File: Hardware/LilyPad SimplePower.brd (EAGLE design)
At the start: 28.4 x 28.4 mm, 16 parts, among them U1 MCP73831

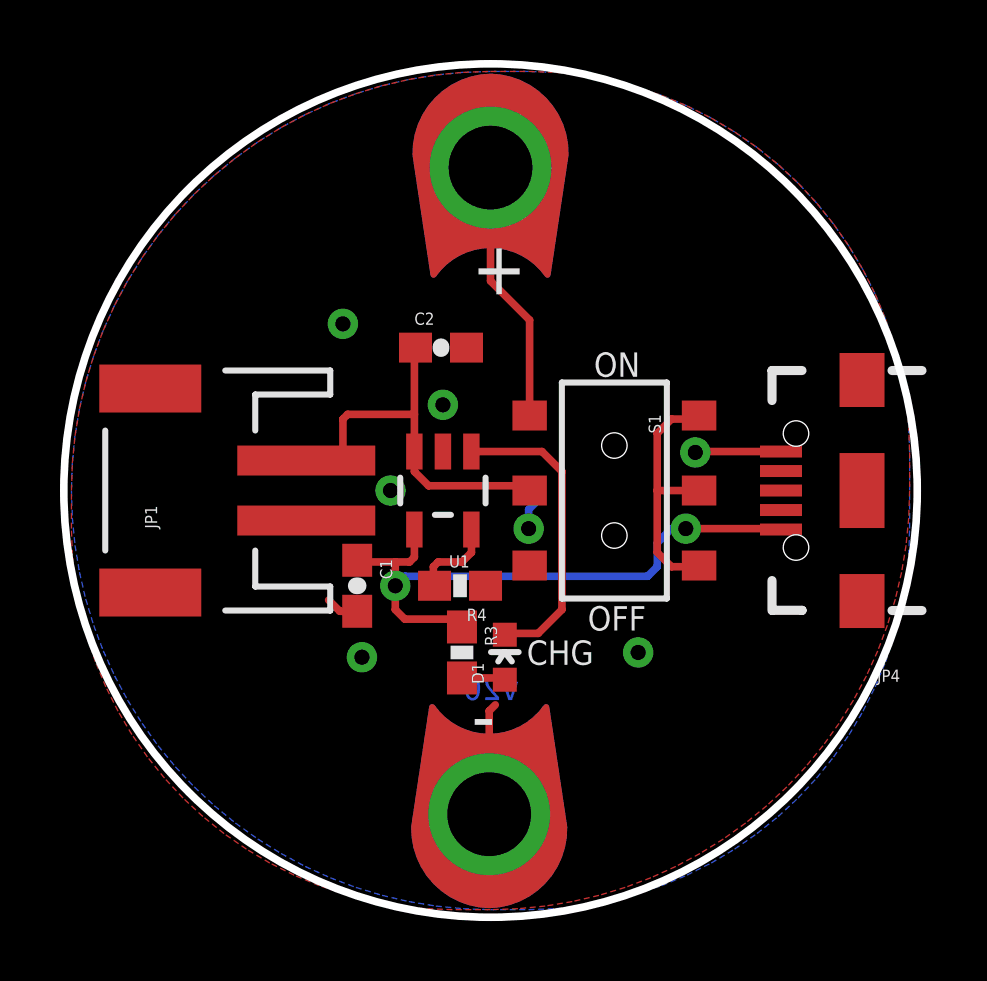
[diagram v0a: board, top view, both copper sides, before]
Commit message: Updating round two protos again to fix missing drill hits.
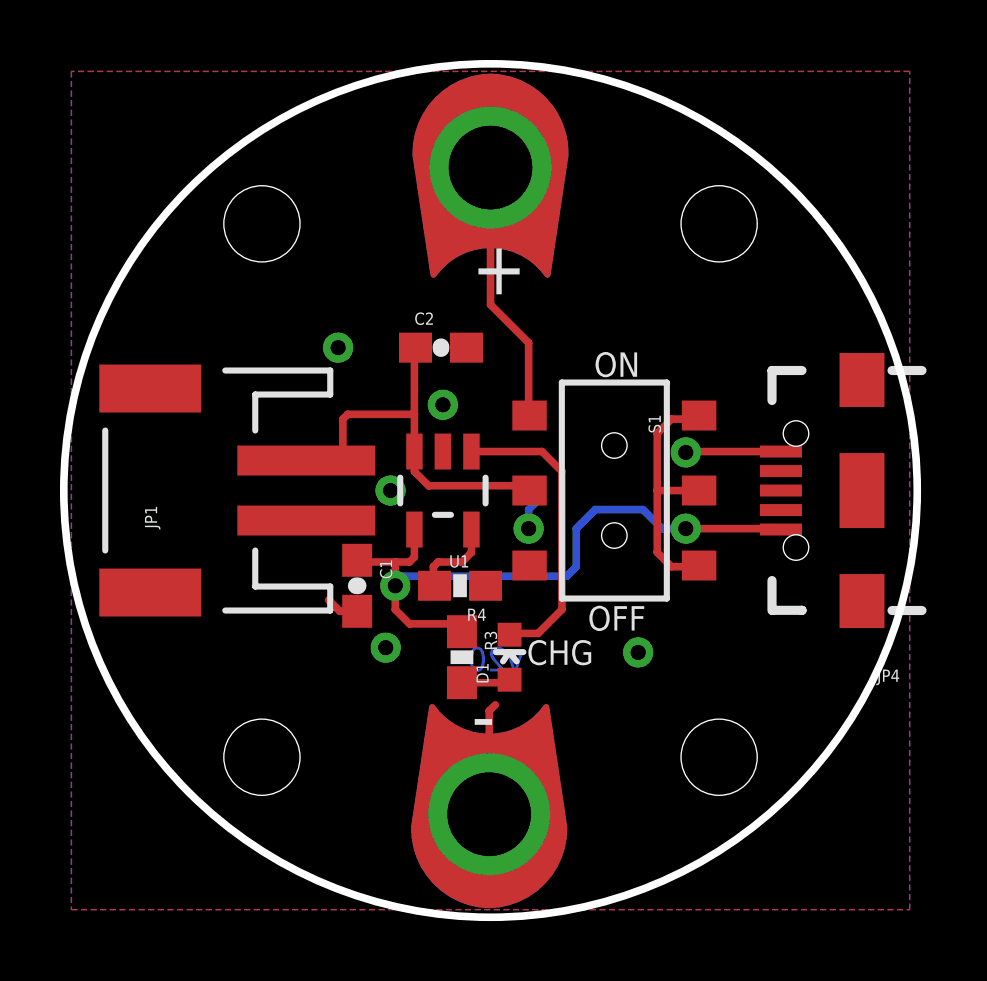
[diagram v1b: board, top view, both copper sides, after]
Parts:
- added STANDOFF1, STANDOFF2, STANDOFF3, STANDOFF4: SEW-HOLE-NO-PAD, Local Library:SEW-HOLE-NO-PAD
- moved JP3 7.68 mm to (-1.11, -5.24)
- moved U$5 6.94 mm to (1.27, -3.81)
- moved U$1 0.32 mm to (0.00, 0.95)
- moved D1 0.16 mm to (0.64, -8.10)
- moved R3 0.16 mm to (-0.95, -8.10)
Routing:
- net GND: track 7.64 -> 11.9 mm
- net N$3: track 21.1 -> 22.0 mm

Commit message: added board fiducials
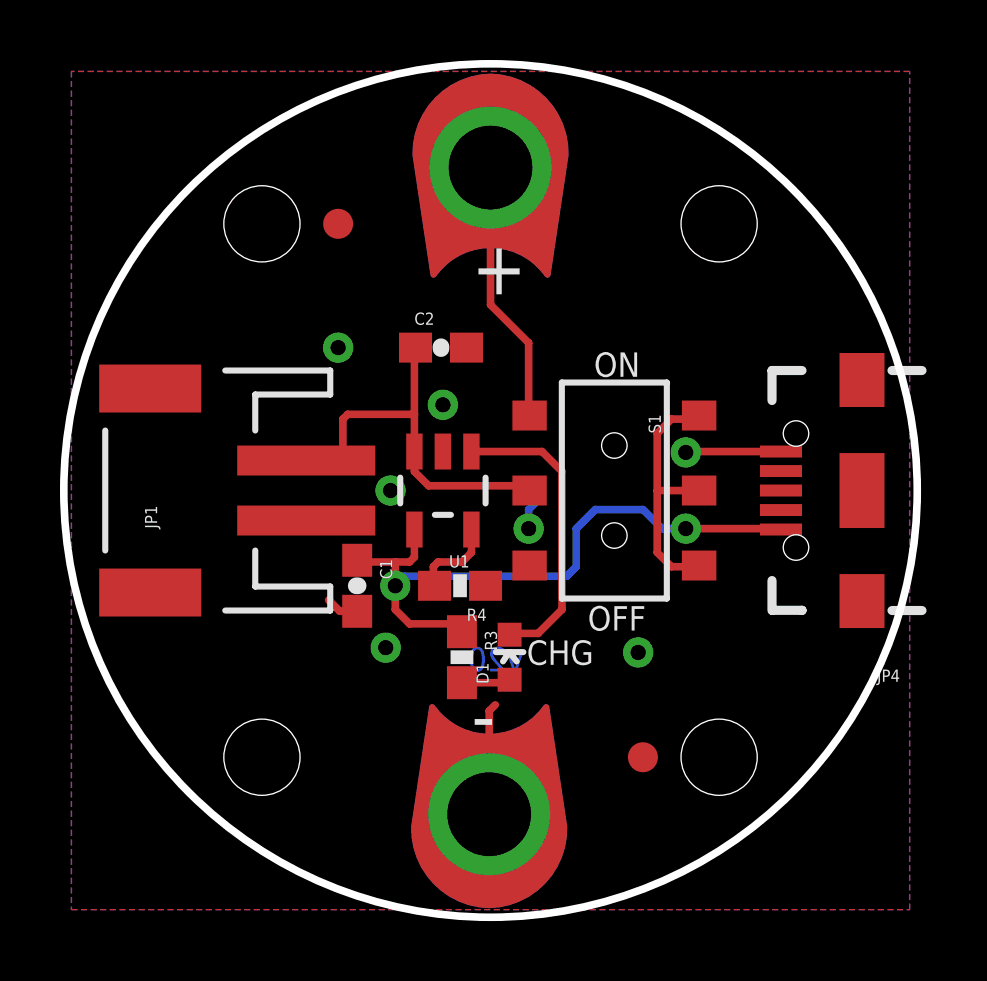
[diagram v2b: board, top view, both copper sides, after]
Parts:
- added FID1, FID2: FIDUCIAL1X2, SparkFun-Aesthetics:FIDUCIAL-1X2
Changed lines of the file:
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@@
 <setting verticaltext="up"/>
 </settings>
-<grid distance="0.00625" unitdist="inch" unit="inch" style="lines" multiple="1" display="yes" altdistance="0.005" altunitdist="inch" altunit="inch"/>
+<grid distance="0.05" unitdist="inch" unit="inch" style="lines" multiple="1" display="yes" altdistance="0.01" altunitdist="inch" altunit="inch"/>
 <layers>
 <layer number="1" name="Top" color="4" fill="1" visible="yes" active="yes"/>
@@
 <layer number="18" name="Vias" color="2" fill="1" visible="yes" active="yes"/>
 <layer number="19" name="Unrouted" color="6" fill="1" visible="yes" active="yes"/>
-<layer number="20" name="Dimension" color="15" fill="1" visible="yes" active="yes"/>
-<layer number="21" name="tPlace" color="16" fill="1" visible="yes" active="yes"/>
-<layer number="22" name="bPlace" color="14" fill="1" visible="yes" active="yes"/>
+<layer number="20" name="Dimension" color="6" fill="1" visible="yes" active="yes"/>
+<layer number="21" name="tPlace" color="6" fill="1" visible="yes" active="yes"/>
+<layer number="22" name="bPlace" color="6" fill="1" visible="yes" active="yes"/>
 <layer number="23" name="tOrigins" color="15" fill="1" visible="yes" active="yes"/>
 <layer number="24" name="bOrigins" color="15" fill="1" visible="yes" active="yes"/>
@@
 <layer number="47" name="Measures" color="7" fill="1" visible="no" active="yes"/>
 <layer number="48" name="Document" color="7" fill="1" visible="no" active="yes"/>
-<layer number="49" name="Reference" color="7" fill="1" visible="yes" active="yes"/>
+<layer number="49" name="Reference" color="7" fill="1" visible="no" active="yes"/>
 <layer number="50" name="dxf" color="7" fill="1" visible="no" active="yes"/>
 <layer number="51" name="tDocu" color="6" fill="1" visible="yes" active="yes"/>
@@
 <element name="STANDOFF3" library="Local Library" package="SEW-HOLE-NO-PAD" value="SEW-HOLE-NO-PAD" x="7.62" y="-11.43"/>
 <element name="STANDOFF4" library="Local Library" package="SEW-HOLE-NO-PAD" value="SEW-HOLE-NO-PAD" x="-7.62" y="-11.43"/>
+<element name="FID1" library="SparkFun-Aesthetics" package="FIDUCIAL-1X2" value="FIDUCIAL1X2" x="-5.08" y="6.35"/>
+<element name="FID2" library="SparkFun-Aesthetics" package="FIDUCIAL-1X2" value="FIDUCIAL1X2" x="5.08" y="-11.43"/>
 </elements>
 <signals>

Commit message: Fixing short, updating parts to match QC checklist
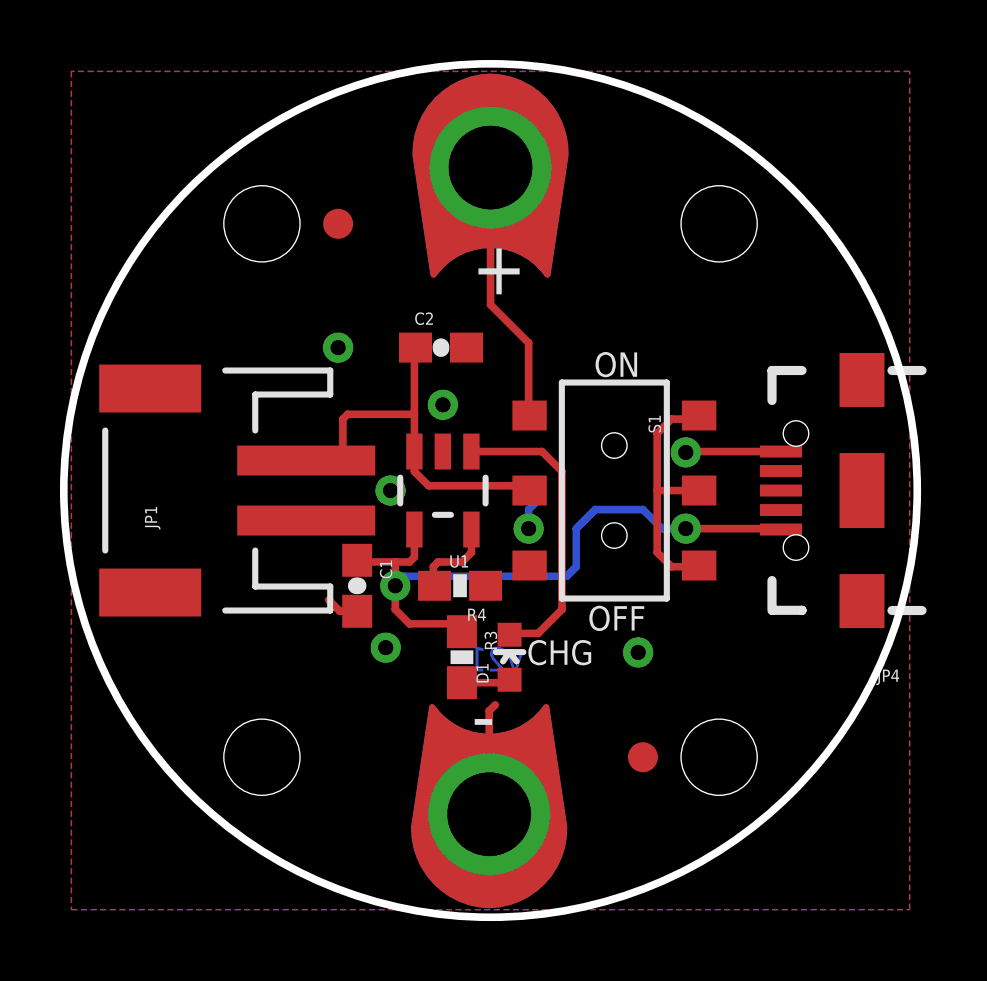
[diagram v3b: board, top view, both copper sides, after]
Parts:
- JP1: value (none) -> M02-JST-2MM-SMT; device SparkFun:JST-2-SMD -> SparkFun-Connectors:JST-2-SMD
- S1: value Power -> DPDT; device SparkFun:AYZ0202 -> SparkFun-Electromechanical:AYZ0202
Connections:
- net N$6 renamed VCC
- net GND: no longer S1.6
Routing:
- net GND: track 11.9 -> 10.7 mm
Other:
- board text added: "v21"
- board text removed: "v20"
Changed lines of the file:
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@@
 <?xml version="1.0" encoding="utf-8"?>
 <!DOCTYPE eagle SYSTEM "eagle.dtd">
-<eagle version="6.6.0">
+<eagle version="7.2.0">
 <drawing>
 <settings>
@@
 <setting verticaltext="up"/>
 </settings>
-<grid distance="0.05" unitdist="inch" unit="inch" style="lines" multiple="1" display="yes" altdistance="0.01" altunitdist="inch" altunit="inch"/>
+<grid distance="0.05" unitdist="inch" unit="inch" style="lines" multiple="1" display="yes" altdistance="0.005" altunitdist="inch" altunit="inch"/>
 <layers>
 <layer number="1" name="Top" color="4" fill="1" visible="yes" active="yes"/>
@@
 <layer number="18" name="Vias" color="2" fill="1" visible="yes" active="yes"/>
 <layer number="19" name="Unrouted" color="6" fill="1" visible="yes" active="yes"/>
-<layer number="20" name="Dimension" color="6" fill="1" visible="yes" active="yes"/>
-<layer number="21" name="tPlace" color="6" fill="1" visible="yes" active="yes"/>
-<layer number="22" name="bPlace" color="6" fill="1" visible="yes" active="yes"/>
+<layer number="20" name="Dimension" color="15" fill="1" visible="yes" active="yes"/>
+<layer number="21" name="tPlace" color="16" fill="1" visible="yes" active="yes"/>
+<layer number="22" name="bPlace" color="14" fill="1" visible="yes" active="yes"/>
 <layer number="23" name="tOrigins" color="15" fill="1" visible="yes" active="yes"/>
 <layer number="24" name="bOrigins" color="15" fill="1" visible="yes" active="yes"/>
@@
 <layer number="47" name="Measures" color="7" fill="1" visible="no" active="yes"/>
 <layer number="48" name="Document" color="7" fill="1" visible="no" active="yes"/>
-<layer number="49" name="Reference" color="7" fill="1" visible="no" active="yes"/>
+<layer number="49" name="Reference" color="7" fill="1" visible="yes" active="yes"/>
 <layer number="50" name="dxf" color="7" fill="1" visible="no" active="yes"/>
 <layer number="51" name="tDocu" color="6" fill="1" visible="yes" active="yes"/>
@@
 <layer number="56" name="wert" color="7" fill="1" visible="no" active="yes"/>
 <layer number="57" name="tCAD" color="7" fill="1" visible="no" active="no"/>
+<layer number="90" name="Modules" color="5" fill="1" visible="no" active="no"/>
 <layer number="91" name="Nets" color="2" fill="1" visible="no" active="no"/>
 <layer number="92" name="Busses" color="1" fill="1" visible="no" active="no"/>
@@
 <text x="-0.635" y="4.0005" size="1.778" layer="21" font="vector" ratio="15">+</text>
 <text x="6.35" y="-26.67" size="1.778" layer="51" font="vector">N. Seidle</text>
-<text x="1.11125" y="-8.5725" size="0.8128" layer="16" font="vector" ratio="25" rot="SMR0">v20</text>
+<text x="1.11125" y="-8.5725" size="0.8128" layer="16" font="vector" ratio="25" rot="SMR0">v21</text>
 <circle x="0" y="-2.54" radius="14.224" width="0.254" layer="20"/>
 <text x="1.2065" y="-8.35025" size="0.8128" layer="21" font="vector" ratio="15">CHG</text>
@@
 <wire x1="6.35" y1="-5.55625" x2="6.35" y2="-5.87375" width="0.254" layer="29"/>
 <wire x1="2.06375" y1="5.08" x2="2.06375" y2="4.60375" width="0.254" layer="29"/>
+<dimension x1="0" y1="-16.764" x2="0" y2="11.684" x3="-24.13" y3="-2.54" textsize="1.27" textratio="15" layer="47" dtype="diameter" unit="inch"/>
+<dimension x1="-0.04445" y1="-13.3304" x2="0" y2="8.255" x3="-20.3382125" y3="-2.495865625" textsize="1.27" textratio="15" layer="47" dtype="diameter" unit="inch"/>
+<dimension x1="-9.8425" y1="-2.54" x2="-15.24" y2="-16.51" x3="-16.51" y3="-9.525" textsize="1.27" textratio="15" layer="47" dtype="vertical" unit="inch"/>
+<dimension x1="-7.62" y1="-11.43" x2="7.62" y2="-11.43" x3="0" y3="-19.05" textsize="1.27" textratio="15" layer="47" unit="inch"/>
+<dimension x1="7.62" y1="6.35" x2="7.62" y2="-11.43" x3="19.05" y3="-2.54" textsize="1.778" textratio="15" layer="47" dtype="vertical" unit="inch"/>
 </plain>
 <attributes>
@@
 <pass name="Default">
 <param name="RoutingGrid" value="50mil"/>
+<param name="AutoGrid" value="1"/>
+<param name="Efforts" value="0"/>
+<param name="TopRouterVariant" value="1"/>
 <param name="tpViaShape" value="round"/>
 <param name="PrefDir.1" value="|"/>
@@
 </autorouter>
 <elements>
-<element name="S1" library="SparkFun" package="AYZ0202" value="Power" x="4.1275" y="-2.54" rot="R270"/>
-<element name="JP1" library="SparkFun" package="JST-2-SMD" value="" x="-9.8425" y="-2.54" rot="R90"/>
+<element name="S1" library="SparkFun-Electromechanical" package="AYZ0202" value="DPDT" x="4.1275" y="-2.54" rot="R270">
+<attribute name="PROD_ID" value="SWCH-08179" x="4.1275" y="-2.54" size="1.778" layer="27" rot="R270" display="off"/>
+<attribute name="VALUE" value="DPDT" x="4.1275" y="-2.54" size="1.778" layer="27" rot="R270" display="off"/>
+</element>
+<element name="JP1" library="SparkFun-Connectors" package="JST-2-SMD" value="M02-JST-2MM-SMT" x="-9.8425" y="-2.54" rot="R90">
+<attribute name="PROD_ID" value="CONN-08352" x="-9.8425" y="-2.54" size="1.778" layer="27" rot="R90" display="off"/>
+</element>
 <element name="U$3" library="LilyPad-Wearables" package="PETAL-LONG-1-2SIDE" value="SEWTAP9" x="-0.04445" y="-13.3604" rot="R90"/>
 <element name="U$4" library="LilyPad-Wearables" package="PETAL-LONG-1-2SIDE" value="SEWTAP9" x="0" y="8.255" rot="R270"/>
@@
 <signals>
 <signal name="N$1">
-<contactref element="JP1" pad="2"/>
 <contactref element="S1" pad="5"/>
 <contactref element="C2" pad="1"/>
@@
 <wire x1="-2.06375" y1="-2.38125" x2="1.14375" y2="-2.38125" width="0.254" layer="1"/>
 <wire x1="1.14375" y1="-2.38125" x2="1.3025" y2="-2.54" width="0.254" layer="1"/>
-<wire x1="-6.1425" y1="-1.54" x2="-4.96875" y2="-1.54" width="0.254" layer="1"/>
 <wire x1="-4.96875" y1="-1.54" x2="-4.92125" y2="-1.5875" width="0.254" layer="1"/>
 <wire x1="-4.92125" y1="-1.5875" x2="-4.92125" y2="-0.15875" width="0.254" layer="1"/>
 <wire x1="-4.92125" y1="-0.15875" x2="-4.7625" y2="0" width="0.254" layer="1"/>
 <wire x1="-4.7625" y1="0" x2="-2.5375" y2="0" width="0.254" layer="1"/>
+<contactref element="JP1" pad="2"/>
+<wire x1="-4.96875" y1="-1.54" x2="-6.1425" y2="-1.54" width="0.254" layer="1"/>
 </signal>
 <signal name="SINK1">
@@
 <wire x1="-1.905" y1="-5.676" x2="-1.866" y2="-5.715" width="0.254" layer="1"/>
 </signal>
-<signal name="N$6">
+<signal name="VCC">
 <contactref element="S1" pad="4"/>
 <contactref element="U$4" pad="1"/>
@@
 <signal name="GND">
 <wire x1="0" y1="-11.27125" x2="0" y2="-11.1125" width="0.254" layer="1"/>
-<contactref element="JP1" pad="1"/>
 <contactref element="U$3" pad="1"/>
 <contactref element="JP4" pad="GND1"/>
@@
 <contactref element="C2" pad="2"/>
 <contactref element="R4" pad="1"/>
-<contactref element="S1" pad="6"/>
 <via x="-3.33375" y="-2.54" extent="1-16" drill="0.508"/>
 <via x="-5.08" y="2.2225" extent="1-16" drill="0.508"/>
@@
 <wire x1="-4.445" y1="-6.565" x2="-5.02375" y2="-6.565" width="0.254" layer="1"/>
 <wire x1="-5.02375" y1="-6.565" x2="-5.3975" y2="-6.19125" width="0.254" layer="1"/>
-<wire x1="-5.23875" y1="-3.81" x2="-5.3975" y2="-3.65125" width="0.254" layer="1"/>
-<wire x1="-5.3975" y1="-3.65125" x2="-6.03125" y2="-3.65125" width="0.254" layer="1"/>
-<wire x1="-6.03125" y1="-3.65125" x2="-6.1425" y2="-3.54" width="0.254" layer="1"/>
-<wire x1="-5.23875" y1="-3.81" x2="-5.3975" y2="-3.81" width="0.254" layer="1"/>
 <via x="-3.4925" y="-7.77875" extent="1-16" drill="0.508"/>
 <wire x1="-0.04445" y1="-9.88695" x2="-0.04445" y2="-10.83945" width="0.254" layer="1"/>
@@
 <wire x1="-0.04445" y1="-11.2268" x2="0" y2="-11.27125" width="0.254" layer="1"/>
 <wire x1="6.53875" y1="-1.24" x2="6.50875" y2="-1.27" width="0.254" layer="1"/>
+<contactref element="JP1" pad="1"/>
 </signal>
 </signals>
+<errors>
+</errors>
 </board>
 </drawing>

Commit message: Fixing QC issues
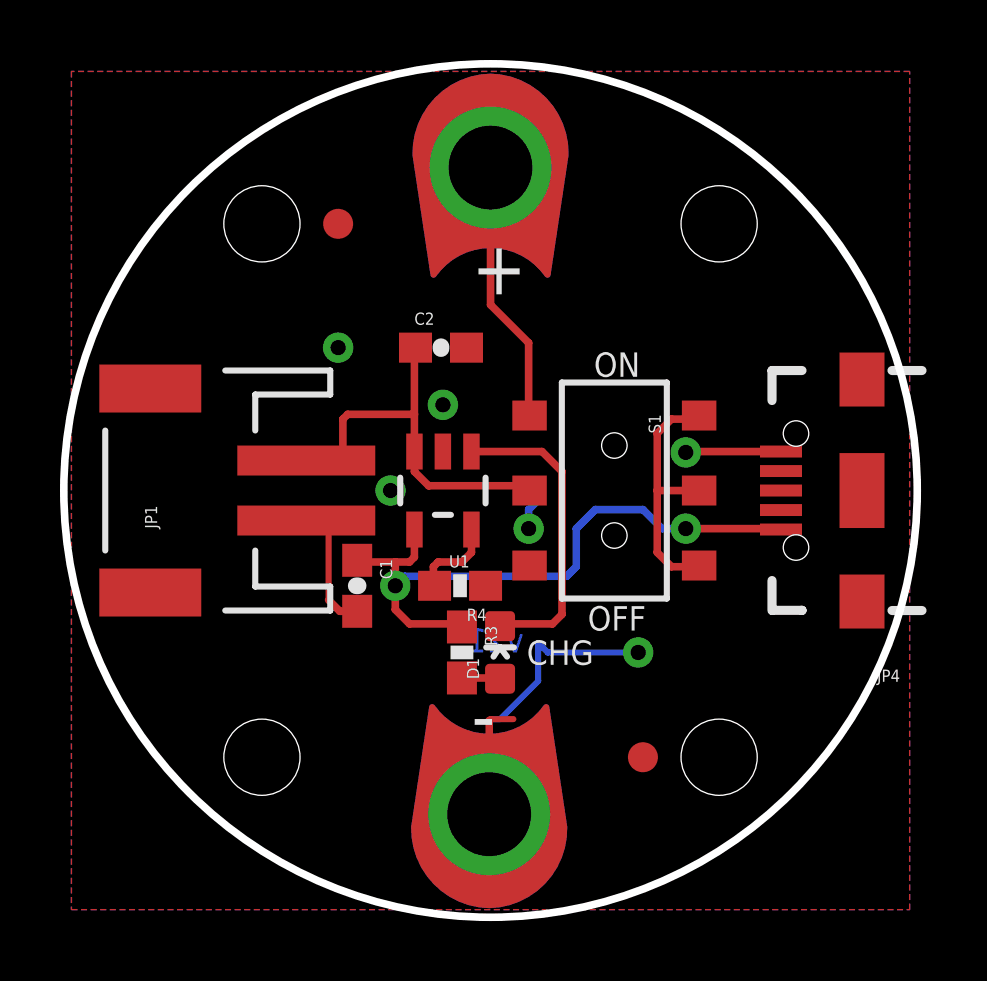
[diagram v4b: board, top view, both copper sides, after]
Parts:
- removed U$3: SEWTAP9, LilyPad-Wearables:PETAL-LONG-1-2SIDE
- added JP5: SFE_LOGO_FLAME.1_INCH, SparkFun-Aesthetics:SFE_LOGO_FLAME_.1
- D1: value (none) -> Yellow
- FRAME1: value FRAME-LETTER -> (none)
- JP3: value LOGO-SFESK -> SEWTAP9; device SparkFun-Aesthetics:SFE-LOGO-FLAME -> LilyPad-Wearables:PETAL-LONG-1-2SIDE
- moved JP3 8.19 mm to (-0.04, -13.4), flipped to the top, turned to 90 degrees
- moved D1 0.35 mm to (0.32, -7.94)
- moved R3 0.16 mm to (-0.95, -7.94)
- renumbered U$4 to JP2
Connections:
- net GND: now also JP3.1; no longer U$3.1
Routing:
- net GND: track 10.7 -> 19.5 mm, vias 7 -> 6
